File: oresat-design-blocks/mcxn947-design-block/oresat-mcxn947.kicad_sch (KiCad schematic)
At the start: 46 parts, among them IC1 MCXN947VKLT, J1 10pin ARM SWD, J2 USB_C_Receptacle_USB2.0_14P, J3 FTDI-UART-6PIN, J4 CAN, J5 TERM, J6 BKUP-BATT, SW1 RESET, SW2 ISP(BOOT), U1 TCAN330, Y1 24M, Y2 830009678

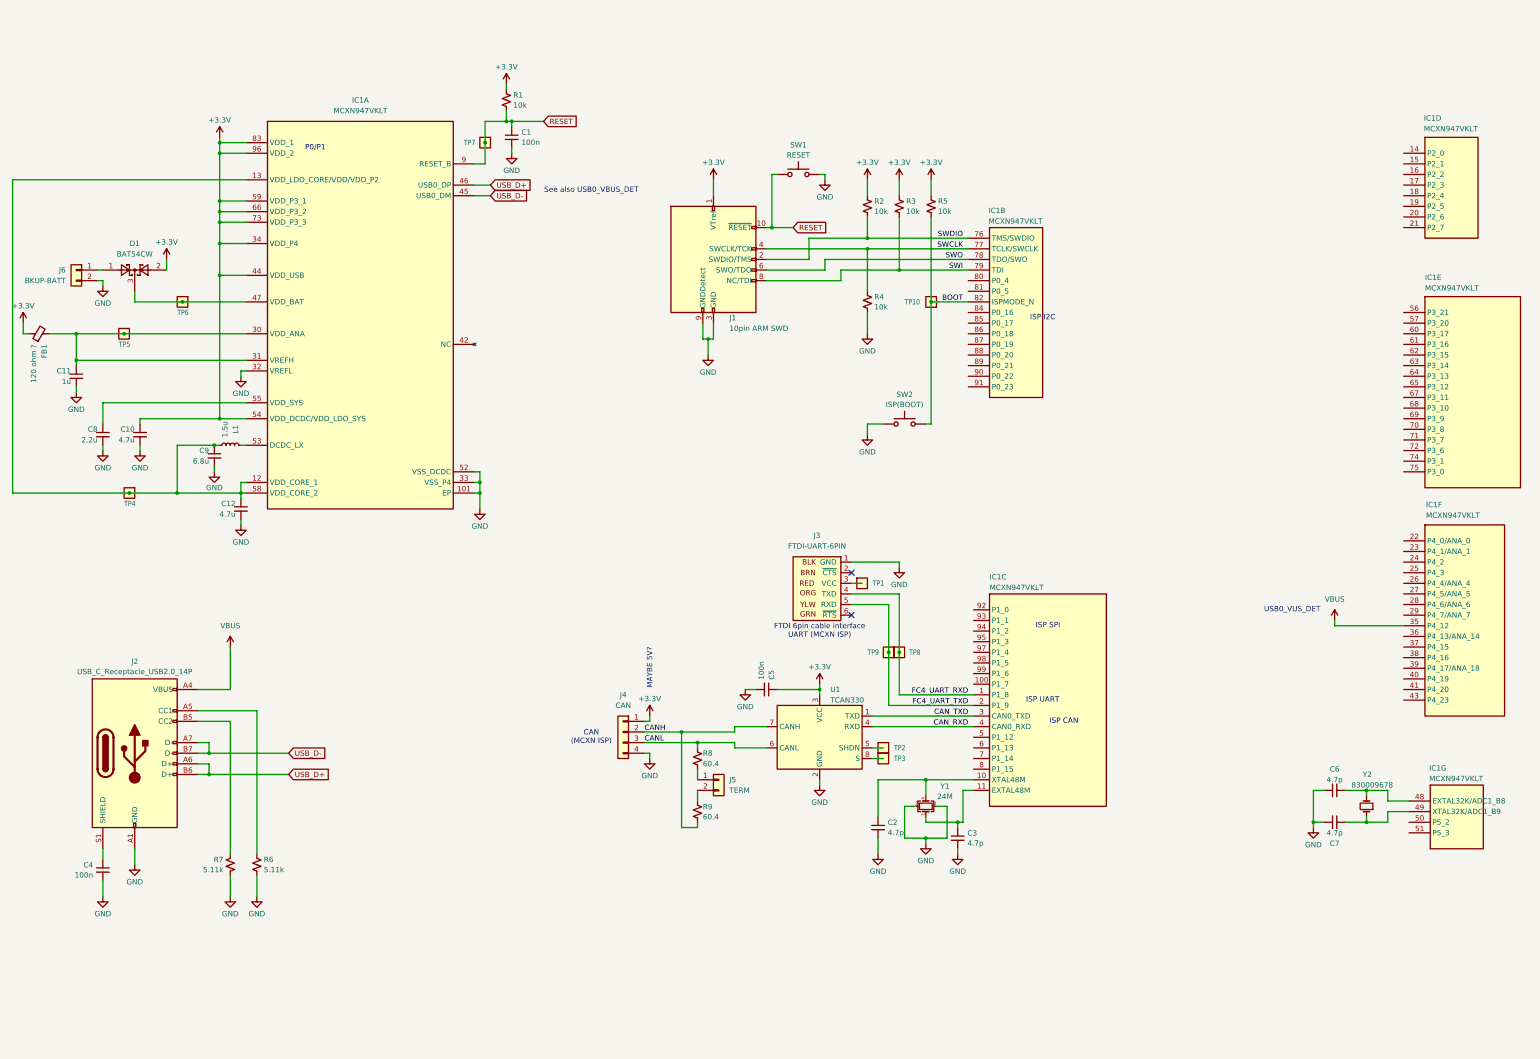
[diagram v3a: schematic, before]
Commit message: Rough draft of schematic done. Power checked against eval board and reference manual. Needs one more go-over we think. Polished symbol, pin names might need another go-around with alt numbers. Added OreSat debug connector because that makes sense. Started 4 layer board layout, initial placements.
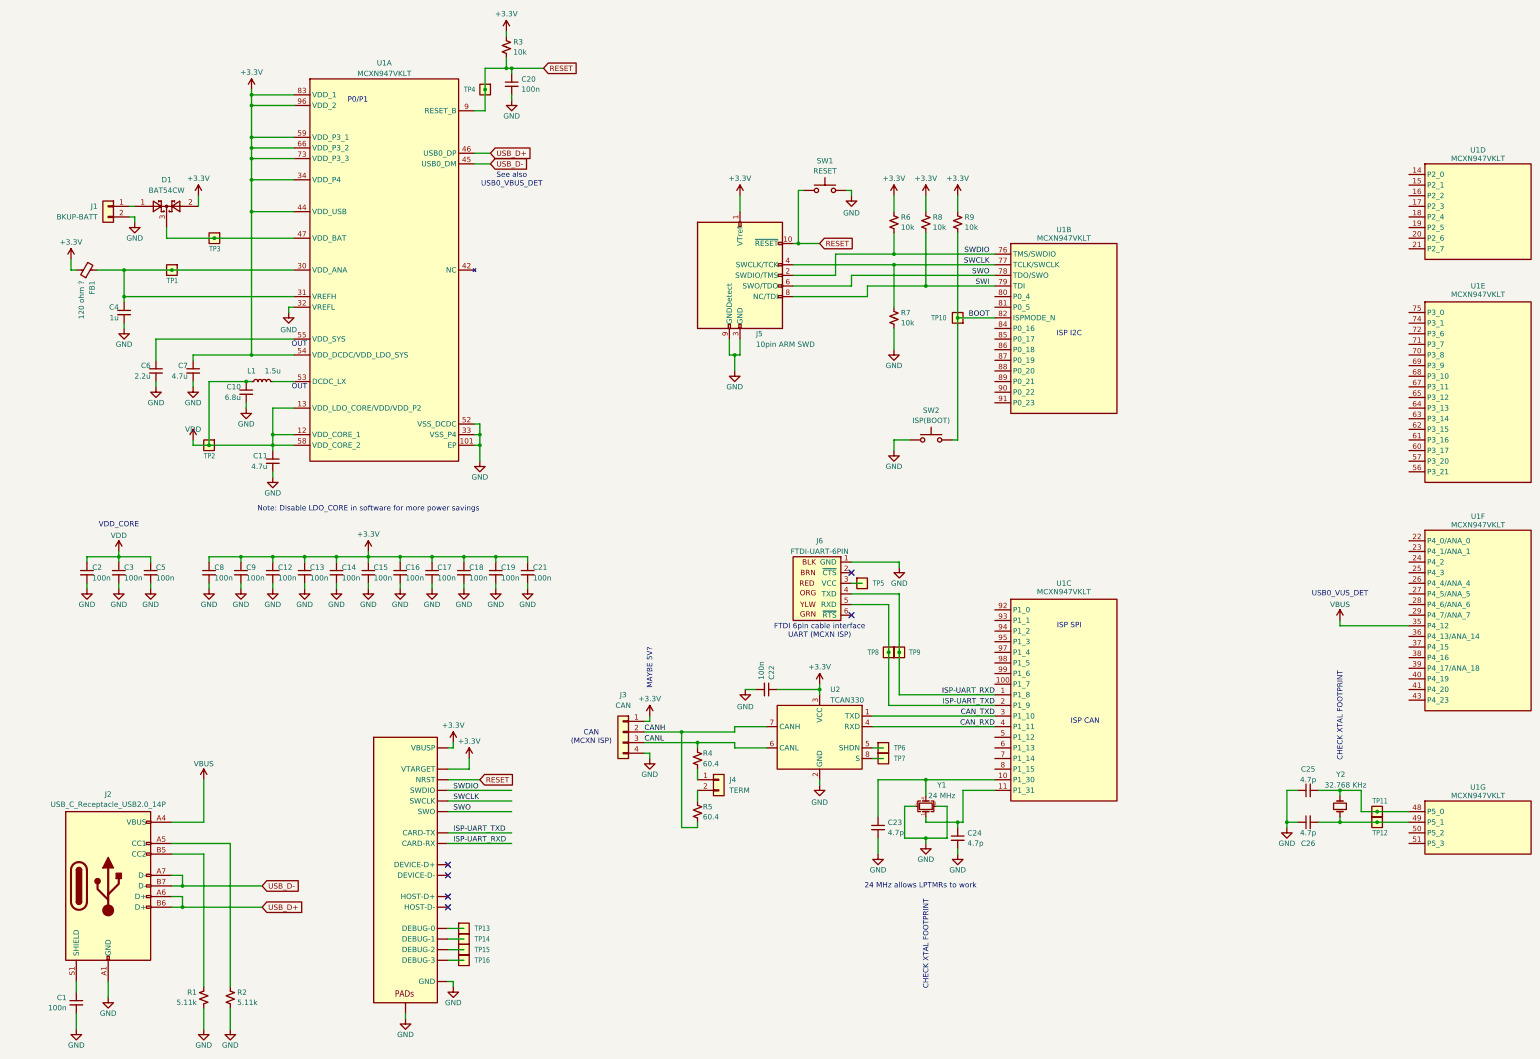
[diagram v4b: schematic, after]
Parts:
- added C12, C13, C14, C15, C16, C17, C18, C19, C2, C21, C3, C5, C8, C9: 100n, oresat-passives:0603-B-NOSILK, symbol Device:C_Small
- added J7: ~, oresat-connectors:J-TE-2-1734592-0, symbol oresat-connectors:ORESAT-DEBUG-CONNECTOR-ALL
- added TP11, TP12, TP13, TP14, TP15, TP16: Test-Point, oresat-misc:TestPoint-0.75mm-th, symbol oresat-misc:Test-Point-0.75mm-th
- C1: renamed from C4; footprint (none) -> oresat-passives:0603-B-NOSILK
- C10: renamed from C9; footprint (none) -> oresat-passives:0603-B-NOSILK
- C11: renamed from C12; footprint (none) -> oresat-passives:0603-B-NOSILK
- C20: renamed from C1; footprint (none) -> oresat-passives:0603-B-NOSILK
- C22: renamed from C5; footprint (none) -> oresat-passives:0603-B-NOSILK
- C23: renamed from C2; footprint (none) -> oresat-passives:0603-B-NOSILK
- C24: renamed from C3; footprint (none) -> oresat-passives:0603-B-NOSILK
- C25: renamed from C6; footprint (none) -> oresat-passives:0603-B-NOSILK
- C26: renamed from C7; footprint (none) -> oresat-passives:0603-B-NOSILK
- C4: renamed from C11; footprint (none) -> oresat-passives:0603-B-NOSILK
- C6: renamed from C8; footprint (none) -> oresat-passives:0603-B-NOSILK
- C7: renamed from C10; footprint (none) -> oresat-passives:0603-B-NOSILK
- D1: footprint Package_TO_SOT_SMD:SOT-323_SC-70 -> oresat-passives:PAT0816(0603)
- FB1: footprint (none) -> oresat-passives:0805-B-NOSILK
- J1: renamed from J6; footprint (none) -> Connector_PinHeader_2.54mm:PinHeader_1x02_P2.54mm_Vertical
- J2: footprint (none) -> Connector_USB:USB_C_Receptacle_Palconn_UTC16-G
- J3: renamed from J4; footprint (none) -> Connector_PinHeader_2.54mm:PinHeader_1x04_P2.54mm_Vertical
- J4: renamed from J5; footprint (none) -> Connector_PinHeader_2.54mm:PinHeader_1x02_P2.54mm_Vertical
- J5: renamed from J1; footprint (none) -> Connector_PinHeader_1.27mm:PinHeader_2x05_P1.27mm_Vertical
- L1: footprint (none) -> Inductor_SMD:L_0805_2012Metric; MFR (none) -> Bourns Inc.; MPN (none) -> SRP2012TMA-1R5M
- R1: renamed from R7; footprint (none) -> oresat-passives:0603-B-NOSILK
- R2: renamed from R6; footprint (none) -> oresat-passives:0603-B-NOSILK
- R3: renamed from R1; footprint (none) -> oresat-passives:0603-B-NOSILK
- R4: renamed from R8; footprint (none) -> oresat-passives:0603-B-NOSILK
- R5: renamed from R9; footprint (none) -> oresat-passives:0603-B-NOSILK
- R6: renamed from R2; footprint (none) -> oresat-passives:0603-B-NOSILK
- R7: renamed from R4; footprint (none) -> oresat-passives:0603-B-NOSILK
- R8: renamed from R3; footprint (none) -> oresat-passives:0603-B-NOSILK
- R9: renamed from R5; footprint (none) -> oresat-passives:0603-B-NOSILK
- U1: renamed from IC1; Arrow Part Number MCXN947VNLT -> (none); Arrow Price/Stock https://www.arrow.com/en/products/mcxn947vnlt/nxp-semicondu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 -> (none); Height 1.6 -> (none); Manufacturer_Name NXP -> (none); Manufacturer_Part_Number MCXN947VNLT -> (none); Mouser Part Number 771-MCXN947VNLT -> (none); Mouser Price/Stock https://www.mouser.co.uk/ProductDetail/NXP-Semiconductors/M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 -> (none)
- U2: renamed from U1; footprint (none) -> Package_TO_SOT_SMD:SOT-23-8
- Y1: value 24M -> 24 MHz; footprint (none) -> Crystal:Crystal_SMD_2016-4Pin_2.0x1.6mm
- Y2: value 830009678 -> 32.768 KHz; footprint (none) -> Crystal:Crystal_SMD_3215-2Pin_3.2x1.5mm; MFR (none) -> Wurth; MPN (none) -> 830009678
- renumbered J3 to J6, TP5 to TP1, TP4 to TP2, TP6 to TP3, TP7 to TP4, TP1 to TP5, TP2 to TP6, TP3 to TP7, TP9 to TP8, TP8 to TP9
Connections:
- net +3.3V: now also C12.1, C13.1, C14.1, C15.1, C16.1, C17.1, C18.1, C19.1, C21.1, C8.1, C9.1, J7.1 (VBUSP), J7.11 (VTARGET), J7.2 (VBUSP)
- net GND: now also C12.2, C13.2, C14.2, C15.2, C16.2, C17.2, C18.2, C19.2, C2.2, C21.2, C3.2, C5.2, C8.2, C9.2, J7.3 (GND), J7.6 (GND), J7.9 (GND), J7.PAD1 (PAD), J7.PAD2 (PAD)
- net RESET: now also J7.10 (NRST)
- net SWCLK: now also J7.15 (SWCLK)
- net SWDIO: now also J7.14 (SWDIO)
- net SWO: now also J7.16 (SWO)
- net VDD: now reaches C10.1, C11.1, L1.1, TP2.1, U1.12 (VDD_CORE_1), U1.13 (VDD_LDO_CORE/VDD/VDD_P2), U1.58 (VDD_CORE_2)
- net VDD: now also C2.1, C3.1, C5.1
- net at C26.2, U1.49 (P5_1), Y2.1: now also TP12.1
- net at C25.2, U1.48 (P5_0), Y2.2: now also TP11.1
- net FC4_UART_RXD renamed ISP-UART_RXD
- net ISP-UART_RXD: now also J7.12 (CARD-RX)
- net FC4_UART_TXD renamed ISP-UART_TXD
- net ISP-UART_TXD: now also J7.13 (CARD-TX)
- new net: J7.17 (DEBUG-0), TP13.1
- new net: J7.18 (DEBUG-1), TP14.1
- new net: J7.19 (DEBUG-2), TP15.1
- new net: J7.20 (DEBUG-3), TP16.1
- no-connect marks 2 -> 6
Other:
- note added: "24 MHz allows LPTMRs to work"
- note added: "CHECK XTAL FOOTPRINT"
- note added: "Note: Disable LDO_CORE in software for more power savings"
- note added: "OUT"
- note added: "VDD_CORE"
- note removed: "ISP UART"
- moved on the sheet: C1, C10, C11, C20, C25, C26, C4, C6, C7, D1, FB1, J1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

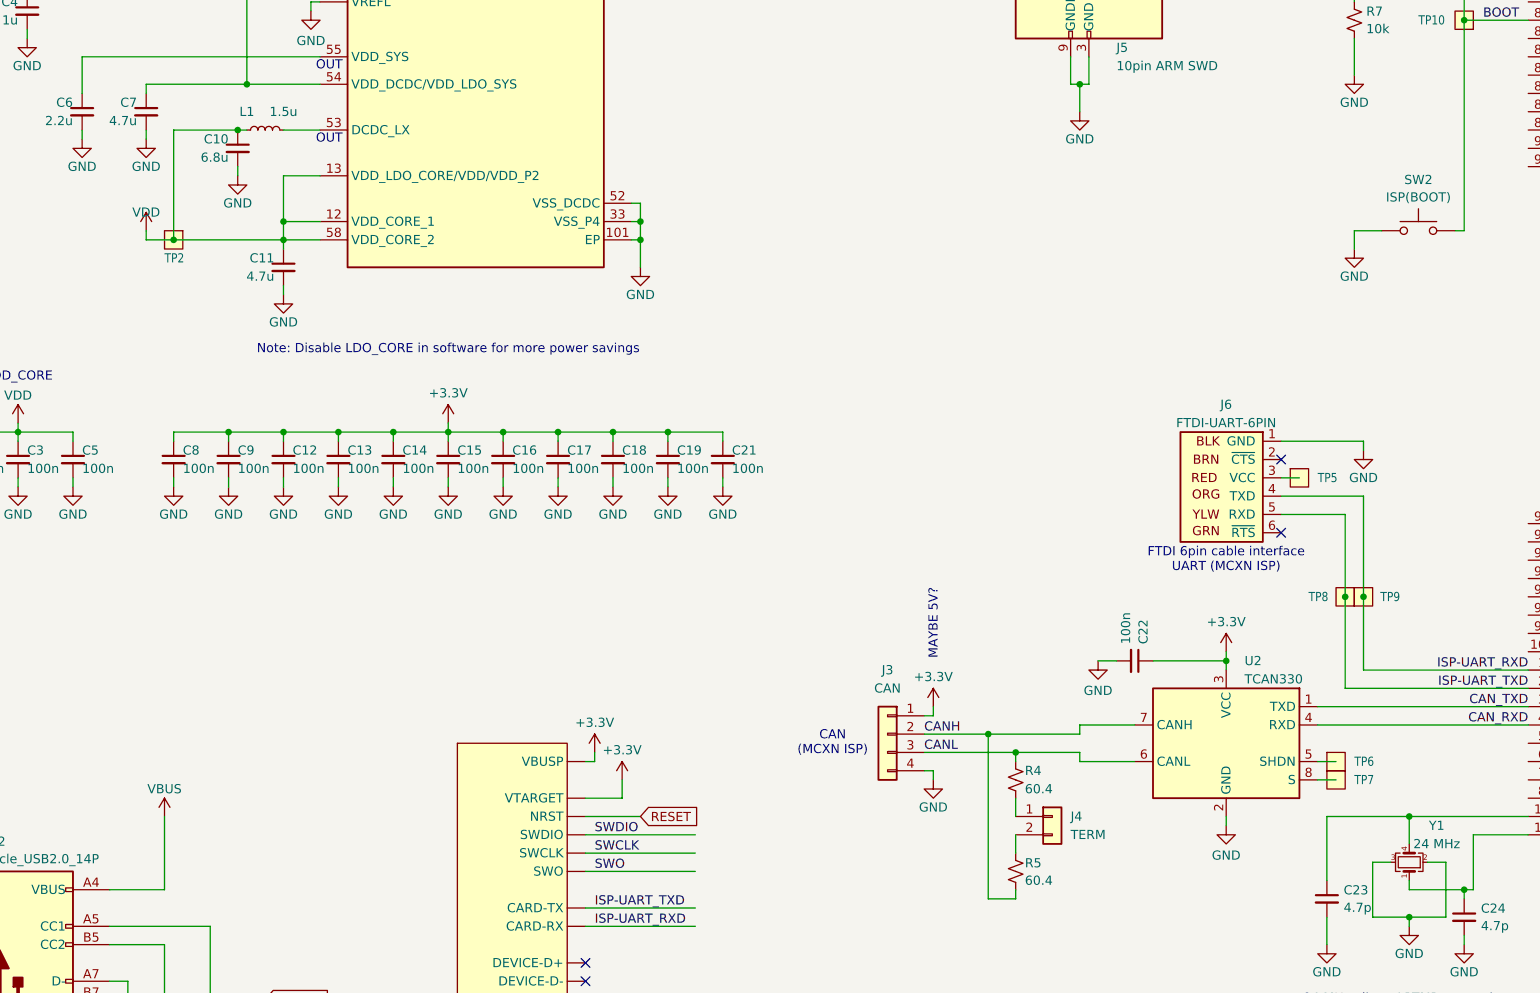
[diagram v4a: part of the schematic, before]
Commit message: More preliminary layout, focusing on power.
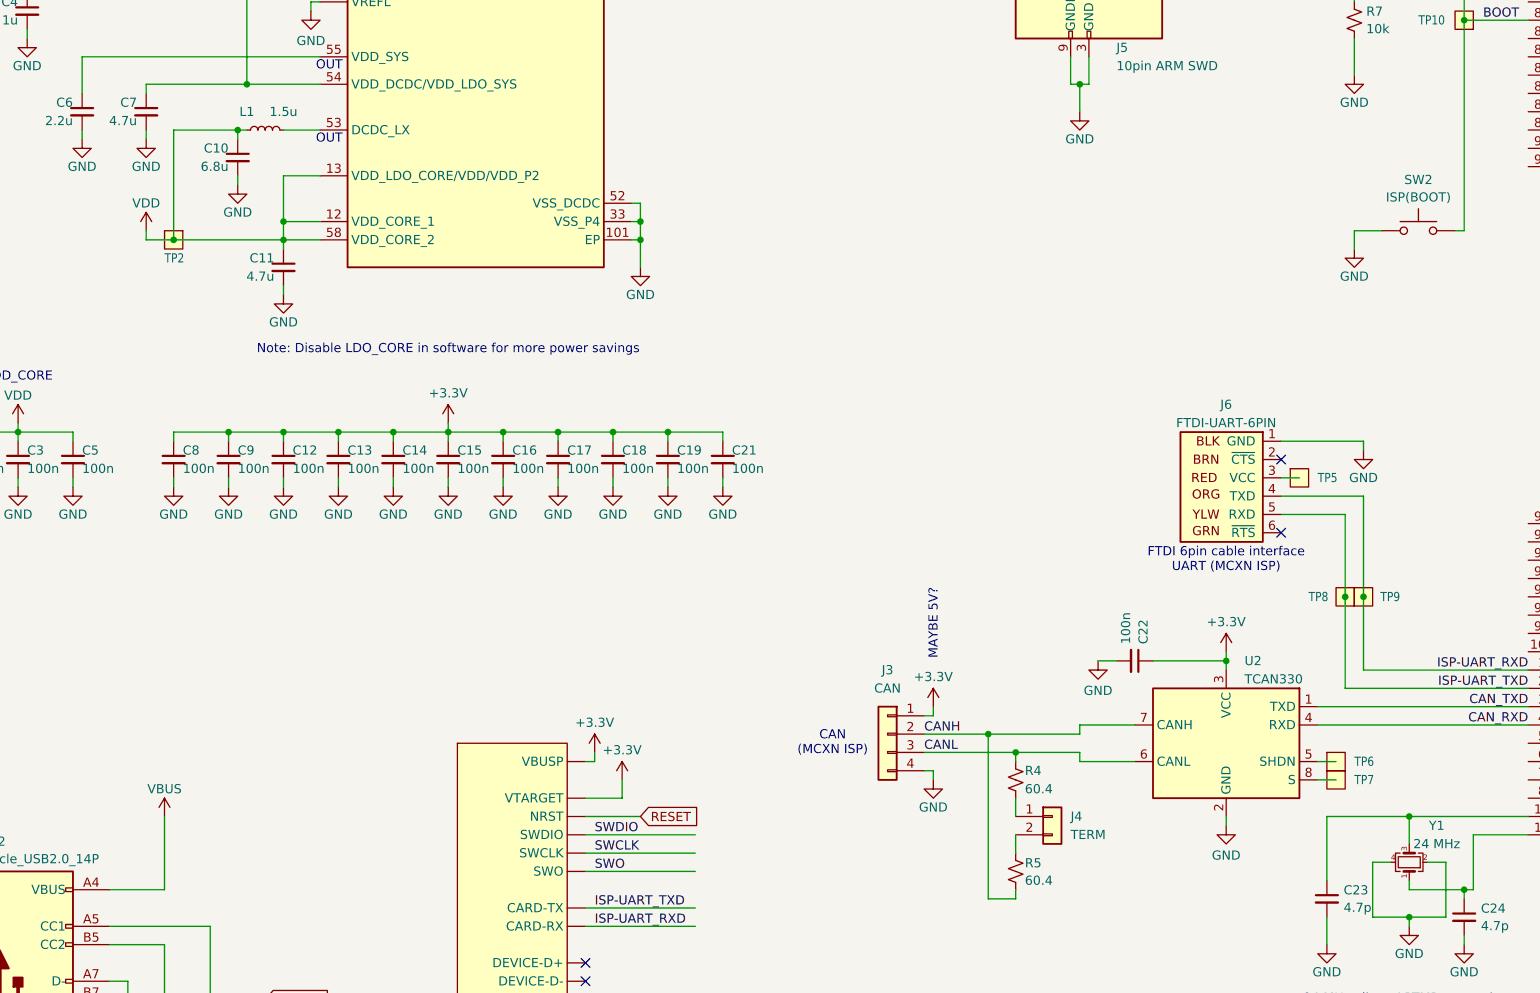
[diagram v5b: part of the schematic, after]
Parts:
- Y1: symbol Device:Crystal_GND23_Small -> Device:Crystal_GND24_Small
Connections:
- net GND: now also Y1.4; no longer Y1.3
- net at C23.1, U1.10 (P1_30): now also Y1.3; no longer Y1.4
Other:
- moved on the sheet: C10
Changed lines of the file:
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@@
 	(wire
 		(pts
+			(xy 77.47 104.14) (xy 77.47 102.87)
+		)
+		(stroke
+			(width 0)
+			(type default)
+		)
+	)
+	(wire
+		(pts
 			(xy 62.23 220.98) (xy 62.23 223.52)
 		)
@@
 	(wire
 		(pts
-			(xy 77.47 107.95) (xy 77.47 109.22)
+			(xy 77.47 109.22) (xy 77.47 110.49)
 		)
 		(stroke
@@
 	(symbol
 		(lib_id "Device:C_Small")
-		(at 77.47 105.41 0)
+		(at 77.47 106.68 0)
 		(mirror y)
 		(unit 1)
@@
 		(dnp no)
 		(property "Reference" "C10"
-			(at 76.2 104.14 0)
+			(at 76.2 105.41 0)
 			(effects
 				(font
@@
 		)
 		(property "Value" "6.8u"
-			(at 76.2 106.68 0)
+			(at 76.2 107.95 0)
 			(effects
 				(font
@@
 		)
 		(property "Footprint" "oresat-passives:0603-B-NOSILK"
-			(at 77.47 105.41 0)
+			(at 77.47 106.68 0)
 			(effects
 				(font
@@
 		)
 		(property "Datasheet" "~"
-			(at 77.47 105.41 0)
+			(at 77.47 106.68 0)
 			(effects
 				(font
@@
 		)
 		(property "Description" "Unpolarized capacitor, small symbol"
-			(at 77.47 105.41 0)
+			(at 77.47 106.68 0)
 			(effects
 				(font
@@
 		)
 		(property "Value" "VDD"
-			(at 64.77 114.3 0)
+			(at 64.77 113.03 0)
 			(effects
 				(font
@@
 	)
 	(symbol
-		(lib_id "Device:Crystal_GND23_Small")
+		(lib_id "Device:Crystal_GND24_Small")
 		(at 240.03 204.47 90)
 		(unit 1)
@@
 			)
 		)
-		(property "Description" "Four pin crystal, GND on pins 2 and 3, small symbol"
+		(property "Description" "Four pin crystal, GND on pins 2 and 4, small symbol"
 			(at 240.03 204.47 0)
 			(effects
@@
 	(symbol
 		(lib_id "power:GND")
-		(at 77.47 109.22 0)
+		(at 77.47 110.49 0)
 		(unit 1)
 		(exclude_from_sim no)
@@
 		(dnp no)
 		(property "Reference" "#PWR019"
-			(at 77.47 115.57 0)
+			(at 77.47 116.84 0)
 			(effects
 				(font
@@
 		)
 		(property "Value" "GND"
-			(at 77.47 113.03 0)
+			(at 77.47 114.3 0)
 			(effects
 				(font
@@
 		)
 		(property "Footprint" ""
-			(at 77.47 109.22 0)
+			(at 77.47 110.49 0)
 			(effects
 				(font
@@
 		)
 		(property "Datasheet" ""
-			(at 77.47 109.22 0)
+			(at 77.47 110.49 0)
 			(effects
 				(font
@@
 		)
 		(property "Description" "Power symbol creates a global label with name \"GND\" , ground"
-			(at 77.47 109.22 0)
+			(at 77.47 110.49 0)
 			(effects
 				(font
